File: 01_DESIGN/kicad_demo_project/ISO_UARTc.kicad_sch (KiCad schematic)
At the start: 3 parts, among them U7 ISO7721DR

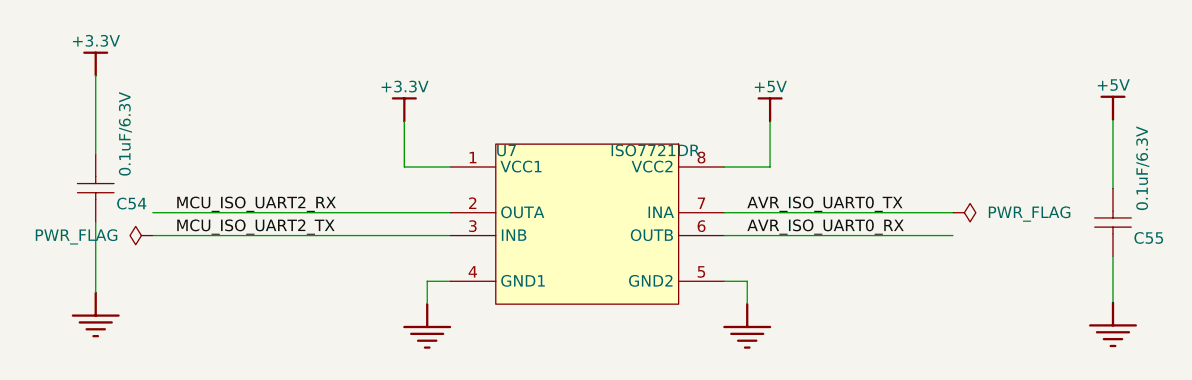
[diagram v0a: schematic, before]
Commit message: Update schematic, PCB
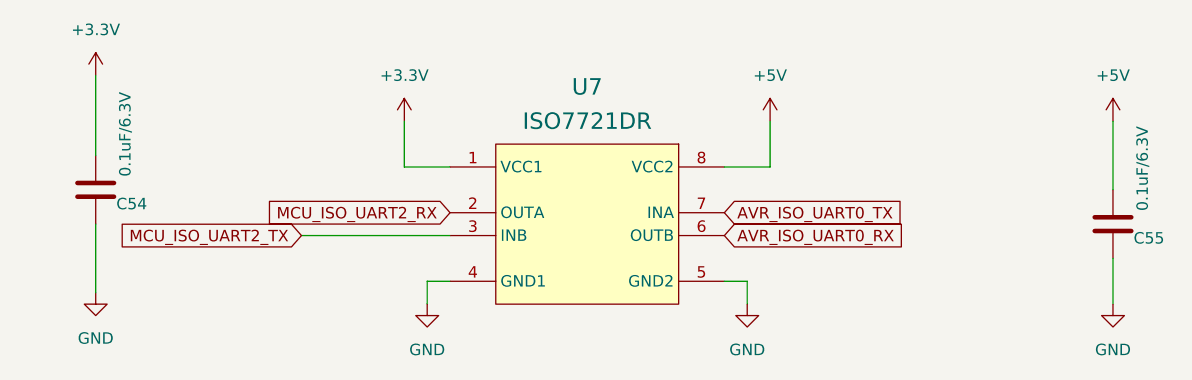
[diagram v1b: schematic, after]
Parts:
- removed U7: ISO7721DR, SOIC127P602X173-8N, symbol ISO7721DR:root_0_ISO7721DR_ISO7721DR.IntLib
- added U7: ISO7721DR, Package_SO:SOIC-8_3.9x4.9mm_P1.27mm, symbol ausb:ISO7721DR
- C54, C55: footprint CAP_C_1608X80 -> Capacitor_SMD:C_0603_1608Metric; symbol Altium_Lib_by_KhueNguyenCreator:root_1_Tu 0402 33nF 10V_Altium_Lib_by_KhueNguyenCreator.IntLib -> Device:C
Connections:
- net +3.3V: now also C54.2, U7.1 (VCC1); no longer C54.1
- net +5V: now also C55.2, U7.8 (VCC2); no longer C55.1
- net AVR_ISO_UART0_RX: now also U7.6 (OUTB)
- net AVR_ISO_UART0_TX: now also U7.7 (INA)
- net GND: now also C54.1, C55.1, U7.4 (GND1), U7.5 (GND2); no longer C54.2, C55.2
- net MCU_ISO_UART2_RX: now also U7.2 (OUTA)
- net MCU_ISO_UART2_TX: now also U7.3 (INB)
